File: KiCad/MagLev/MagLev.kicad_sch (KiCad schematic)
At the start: 60 parts, among them J1 Barrel_Jack, Q12 AOD442G, Q13 AOD442G, Q17 ZX5T851GTA, Q18 ZX5T1951GTA, Q5 ZX5T1951GTA, U10 DRV5505, U11 DRV5505, U12 DRV5505, U13 MCP1402, U14 MCP1402, U3 L78L05_SO8, U4 TL431A, U5 LM393, X1 L_Ferrite, X2 L_Ferrite, Y1 L_Ferrite, Y2 L_Ferrite, Y5 L_Ferrite, Y6 L_Ferrite, Y8 L_Ferrite, Y9 L_Ferrite

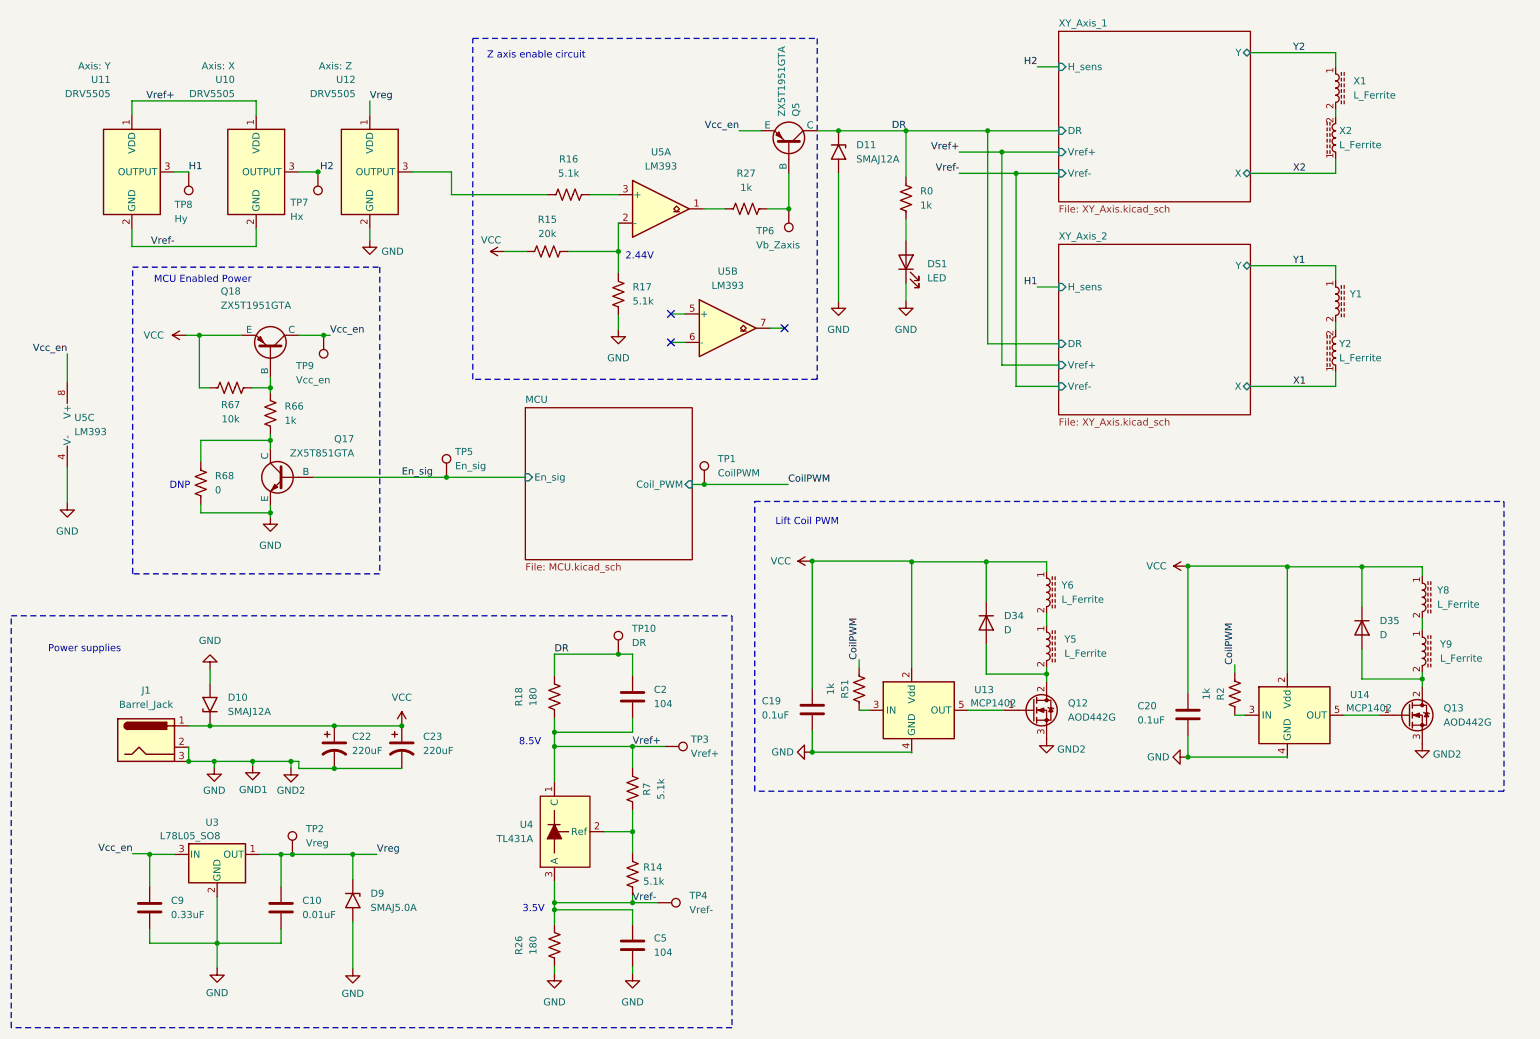
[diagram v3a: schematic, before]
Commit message: Add netclasses, define PCB rules.
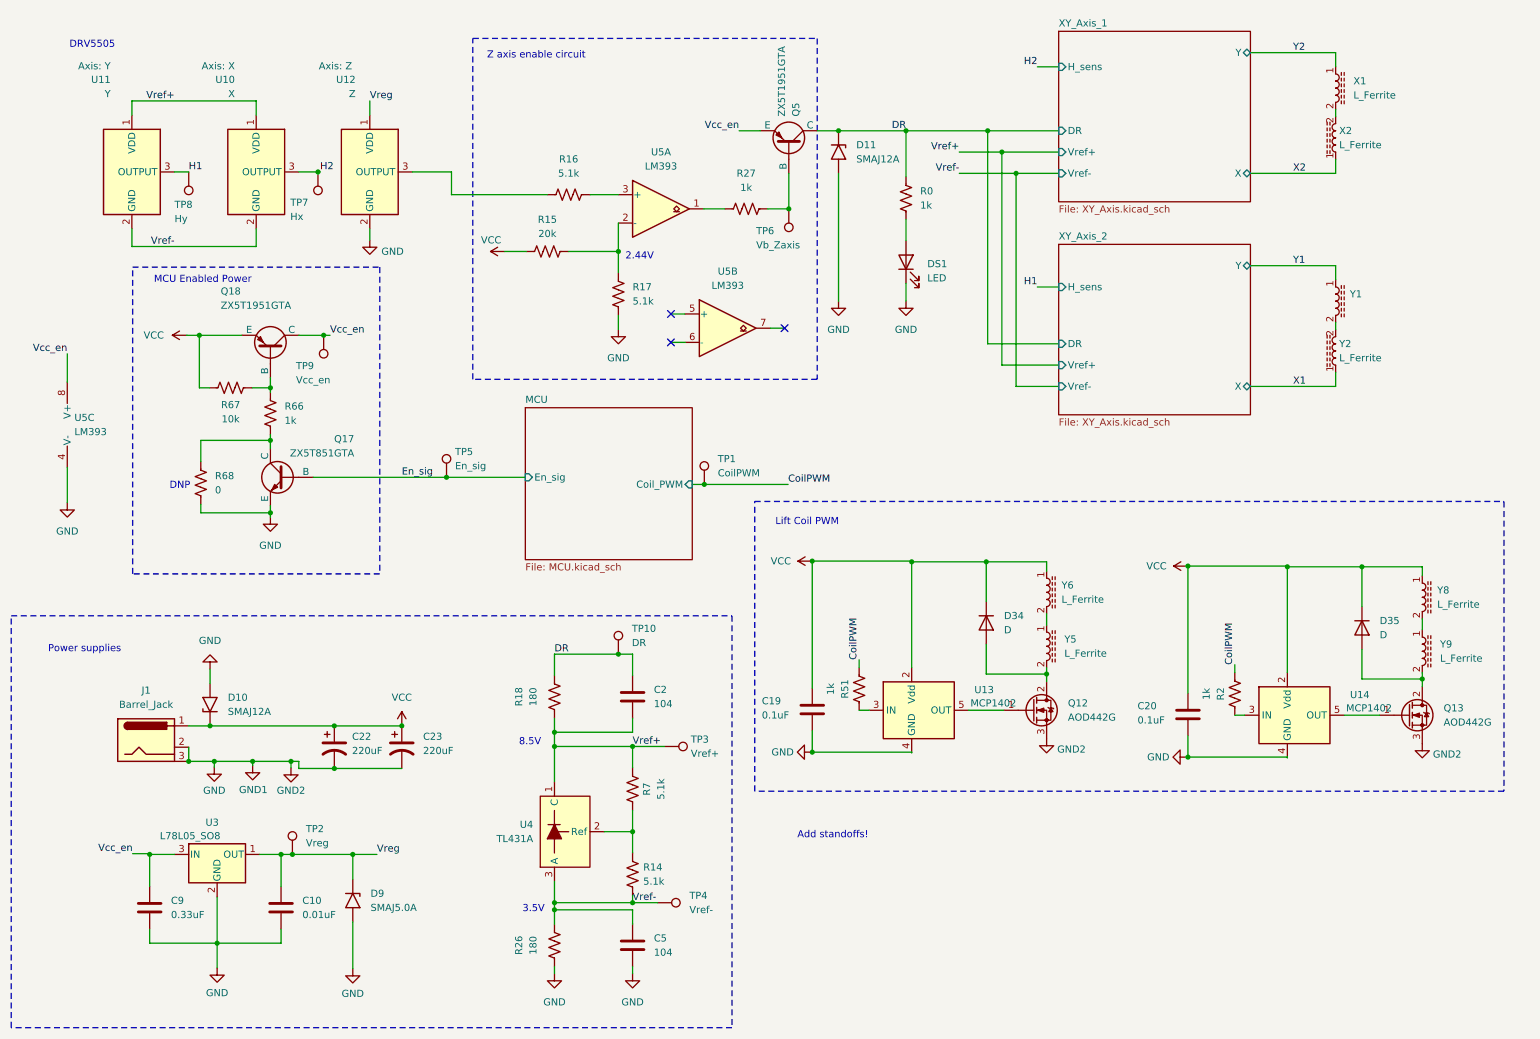
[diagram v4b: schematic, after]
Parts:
- U10: value DRV5505 -> X
- U11: value DRV5505 -> Y
- U12: value DRV5505 -> Z
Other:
- note added: "Add standoffs!"
- note added: "DRV5505"
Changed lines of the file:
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@@
+    (effects (font (size 1.27 1.27)) (justify left bottom))
+  )
+  (text "Add standoffs!" (at 157.734 161.29 0)
     (effects (font (size 1.27 1.27)) (justify left bottom))
   )
@@
     (effects (font (size 1.27 1.27)) (justify left bottom))
   )
+  (text "DRV5505" (at 27.559 19.939 0)
+    (effects (font (size 1.27 1.27)) (justify left bottom))
+  )
   (label "CoilPWM" (at 168.783 129.159 90) (fields_autoplaced)
     (effects (font (size 1.27 1.27)) (justify left bottom))
@@
   (label "DR" (at 114.3 128.143 0) (fields_autoplaced)
     (effects (font (size 1.27 1.27)) (justify left bottom))
+  )
+  (netclass_flag "" (length 2.54) (shape round) (at 70.104 140.97 0) (fields_autoplaced)
+    (effects (font (size 1.27 1.27)) (justify left bottom))
+    (property "Netclass" "Supply" (at 70.8025 138.43 0)
+      (effects (font (size 1.27 1.27) italic) (justify left))
+    )
+  )
+  (netclass_flag "" (length 2.54) (shape round) (at 254 31.369 270)
+    (effects (font (size 1.27 1.27)) (justify right bottom))
+    (property "Netclass" "HighCurrent" (at 257.429 30.48 0)
+      (effects (font (size 1.27 1.27) italic) (justify left))
+    )
+  )
+  (netclass_flag "" (length 2.54) (shape round) (at 69.977 71.12 0)
+    (effects (font (size 1.27 1.27)) (justify left bottom))
+    (property "Netclass" "Supply" (at 70.231 66.929 0)
+      (effects (font (size 1.27 1.27) italic) (justify left))
+    )
+  )
+  (netclass_flag "" (length 2.54) (shape round) (at 191.516 129.667 90) (fields_autoplaced)
+    (effects (font (size 1.27 1.27)) (justify left bottom))
+    (property "Netclass" "HighCurrent" (at 188.976 128.9685 90)
+      (effects (font (size 1.27 1.27) italic) (justify left))
+    )
+  )
+  (netclass_flag "" (length 2.54) (shape round) (at 254 69.342 270)
+    (effects (font (size 1.27 1.27)) (justify right bottom))
+    (property "Netclass" "HighCurrent" (at 257.429 68.453 0)
+      (effects (font (size 1.27 1.27) italic) (justify left))
+    )
+  )
+  (netclass_flag "" (length 2.54) (shape round) (at 269.494 123.444 270)
+    (effects (font (size 1.27 1.27)) (justify right bottom))
+    (property "Netclass" "HighCurrent" (at 271.653 121.92 0)
+      (effects (font (size 1.27 1.27) italic) (justify left))
+    )
+  )
+  (netclass_flag "" (length 2.54) (shape round) (at 202.311 122.428 270)
+    (effects (font (size 1.27 1.27)) (justify right bottom))
+    (property "Netclass" "HighCurrent" (at 204.47 120.904 0)
+      (effects (font (size 1.27 1.27) italic) (justify left))
+    )
+  )
+  (netclass_flag "" (length 2.54) (shape round) (at 168.783 34.544 0)
+    (effects (font (size 1.27 1.27)) (justify left bottom))
+    (property "Netclass" "Supply" (at 169.037 30.353 0)
+      (effects (font (size 1.27 1.27) italic) (justify left))
+    )
+  )
+  (netclass_flag "" (length 2.54) (shape round) (at 258.699 131.572 90) (fields_autoplaced)
+    (effects (font (size 1.27 1.27)) (justify left bottom))
+    (property "Netclass" "HighCurrent" (at 256.159 130.8735 90)
+      (effects (font (size 1.27 1.27) italic) (justify left))
+    )
+  )
+  (netclass_flag "" (length 2.54) (shape round) (at 184.15 111.633 0) (fields_autoplaced)
+    (effects (font (size 1.27 1.27)) (justify left bottom))
+    (property "Netclass" "HighCurrent" (at 184.8485 109.093 0)
+      (effects (font (size 1.27 1.27) italic) (justify left))
+    )
+  )
+  (netclass_flag "" (length 2.54) (shape round) (at 259.842 112.522 0) (fields_autoplaced)
+    (effects (font (size 1.27 1.27)) (justify left bottom))
+    (property "Netclass" "HighCurrent" (at 260.5405 109.982 0)
+      (effects (font (size 1.27 1.27) italic) (justify left))
+    )
   )
   (symbol (lib_id "Device:C_Polarized_US") (at 86.995 144.78 0) (unit 1)
@@
       (effects (font (size 1.27 1.27)) (justify right))
     )
-    (property "Value" "DRV5505" (at 34.925 27.94 0)
+    (property "Value" "Y" (at 34.925 27.94 0)
       (effects (font (size 1.27 1.27)) (justify right))
     )
@@
       (effects (font (size 1.27 1.27)) (justify right))
     )
-    (property "Value" "DRV5505" (at 78.74 27.94 0)
+    (property "Value" "Z" (at 78.74 27.94 0)
       (effects (font (size 1.27 1.27)) (justify right))
     )
@@
       (effects (font (size 1.27 1.27)) (justify right))
     )
-    (property "Value" "DRV5505" (at 57.15 27.94 0)
-      (effects (font (size 1.27 1.27)) (justify right))
-    )
+    (property "Value" "X" (at 57.15 27.94 0)
+      (effects (font (size 1.27 1.27)) (justify right))
+    )

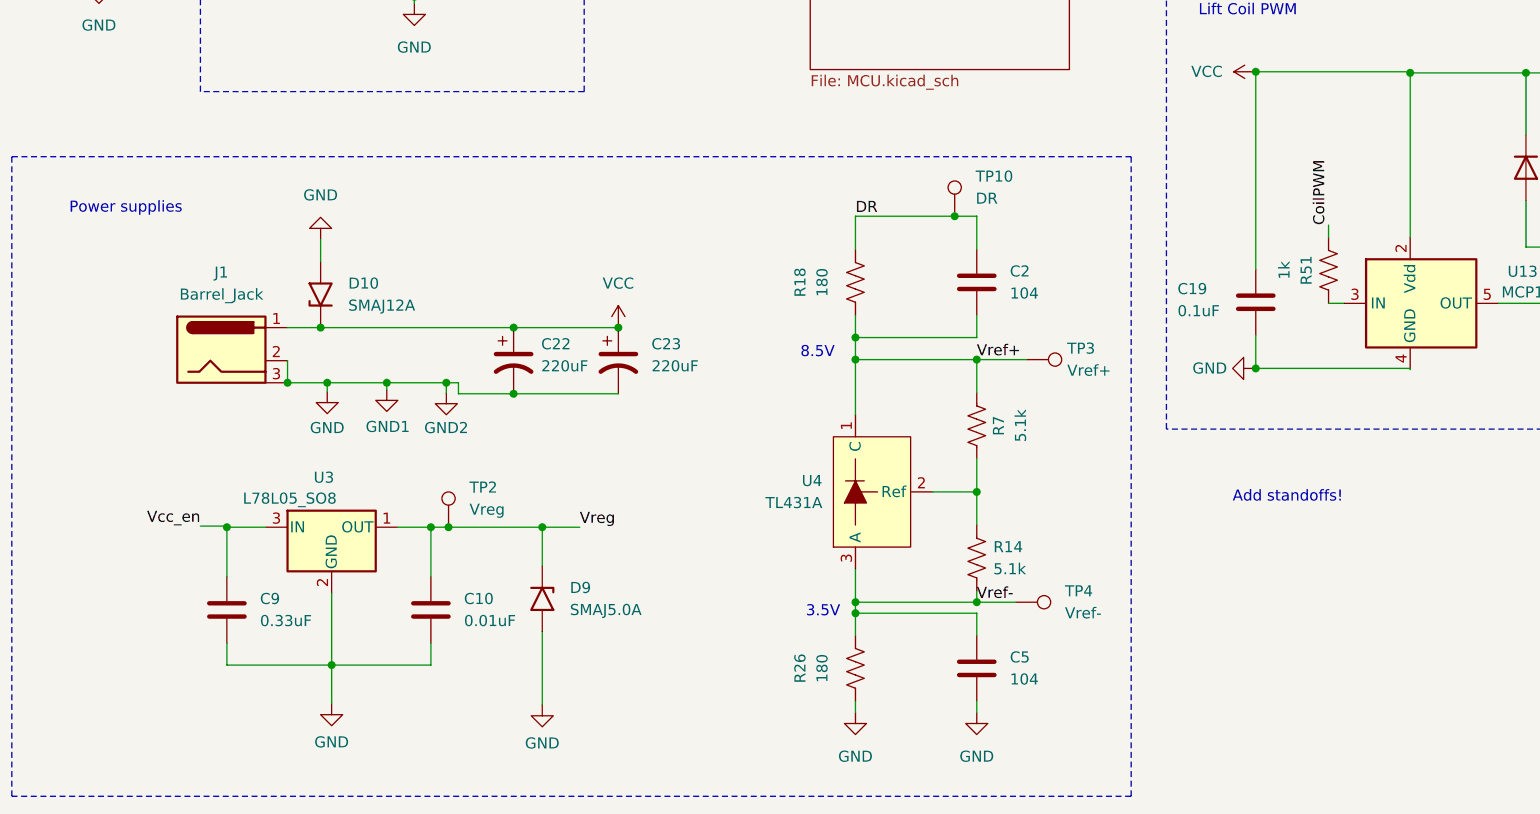
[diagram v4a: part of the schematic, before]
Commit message: Place and route MCU page components.
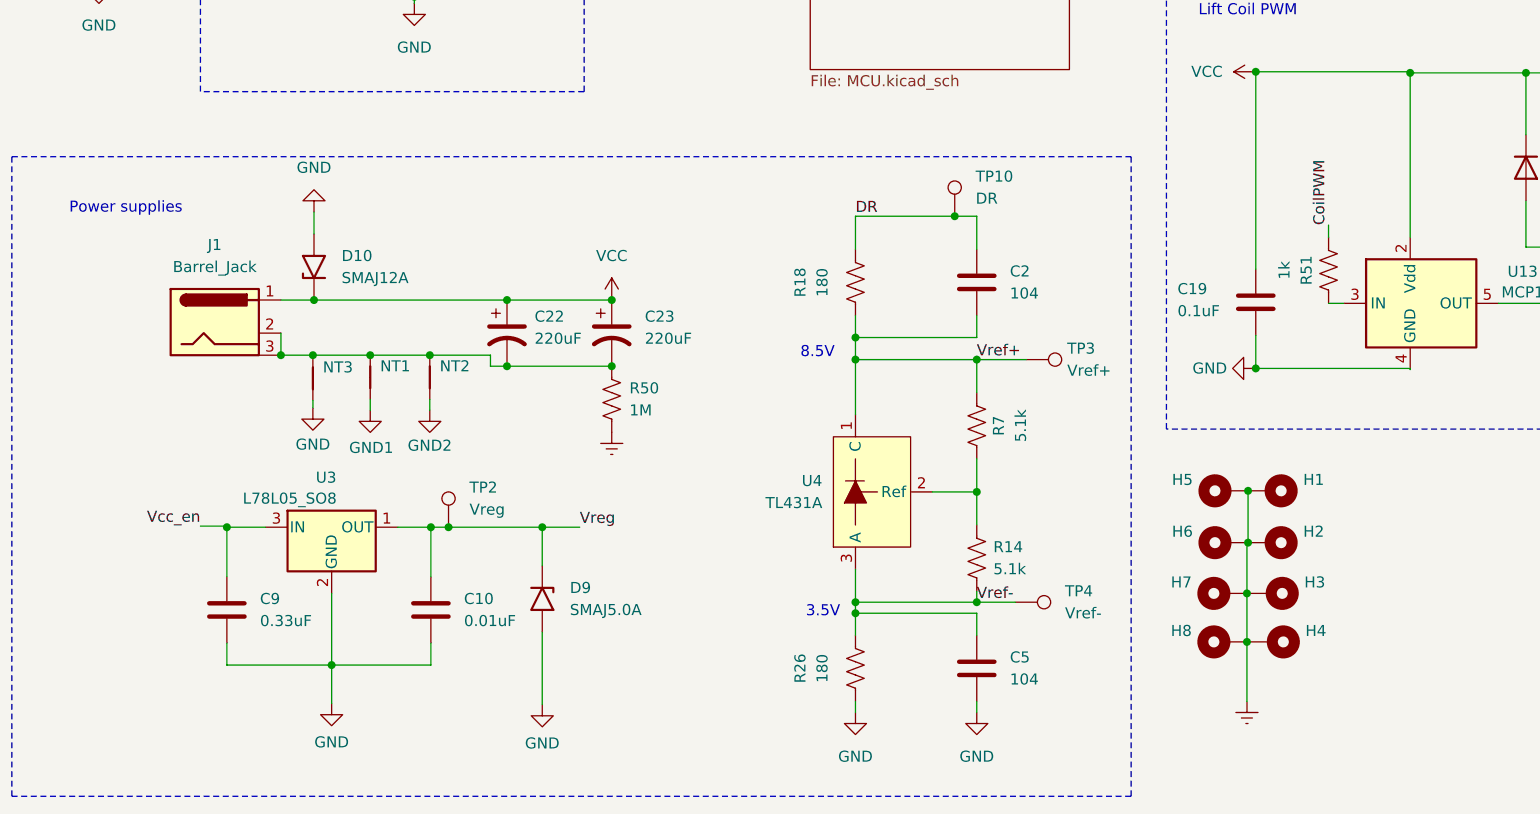
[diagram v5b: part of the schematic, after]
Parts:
- added H1, H2, H3, H4, H5, H6, H7, H8: MountingHole_Pad, MountingHole:MountingHole_3.2mm_M3_Pad, symbol Mechanical:MountingHole_Pad
- added NT1, NT2: NetTie_2, NetTie:NetTie-2_SMD_Pad2.0mm, symbol Device:NetTie_2
- added NT3: NetTie_2, NetTie:NetTie-2_SMD_Pad0.5mm, symbol Device:NetTie_2
- added R50: 1M, Resistor_SMD:R_0805_2012Metric_Pad1.20x1.40mm_HandSolder, symbol Device:R_US
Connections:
- net GND: now also NT3.2; no longer C22.2, C23.2, J1.2, J1.3, Q12.3 (S), Q13.3 (S)
- new net: C22.2, C23.2, J1.2, J1.3, NT1.1, NT2.1, NT3.1, R50.1
- new net Earth: H1.1, H2.1, H3.1, H4.1, H5.1, H6.1, H7.1, H8.1, R50.2
- new net GND1: NT1.2
- new net GND2: NT2.2, Q12.3 (S), Q13.3 (S)
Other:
- note removed: "Add standoffs!"
- moved on the sheet: C22, C23, D10, J1
